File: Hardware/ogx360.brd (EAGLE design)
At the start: 97.1 x 36.5 mm, 29 parts, among them J1 USB_A_SMT_FEMALE_NS, SW1 TL3305AF160QG, U1 MAX3421ETQFP32-5MM, U2 74HC4050, U3 MIC5219-3.3YM5-TR, U4 ARDUINO_LEONARDO_MICRO, U5 ARDUINO_LEONARDO_MICRO, U6 ARDUINO_LEONARDO_MICRO, U7 ARDUINO_LEONARDO_MICRO, Y1 12MHz

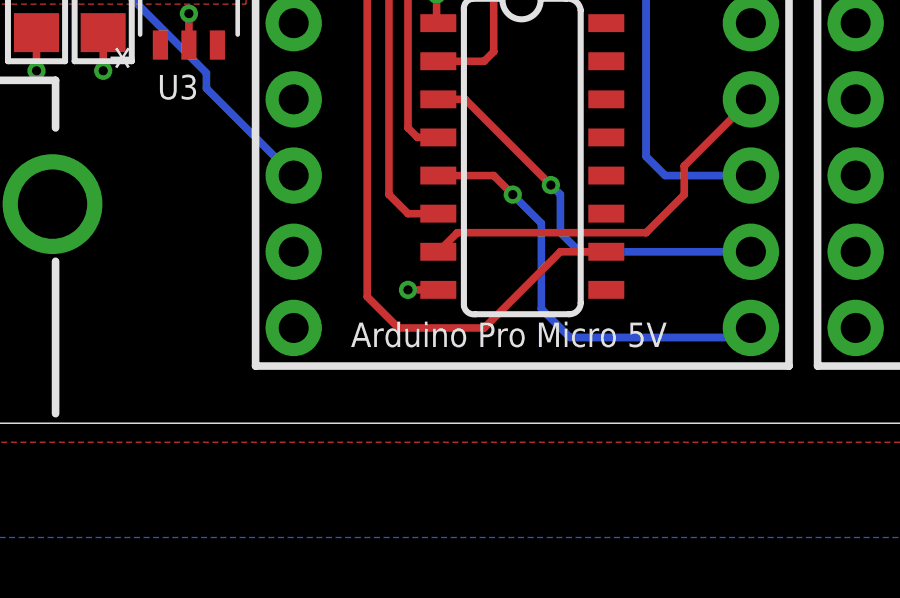
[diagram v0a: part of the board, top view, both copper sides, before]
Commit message: HW: Route reset trace
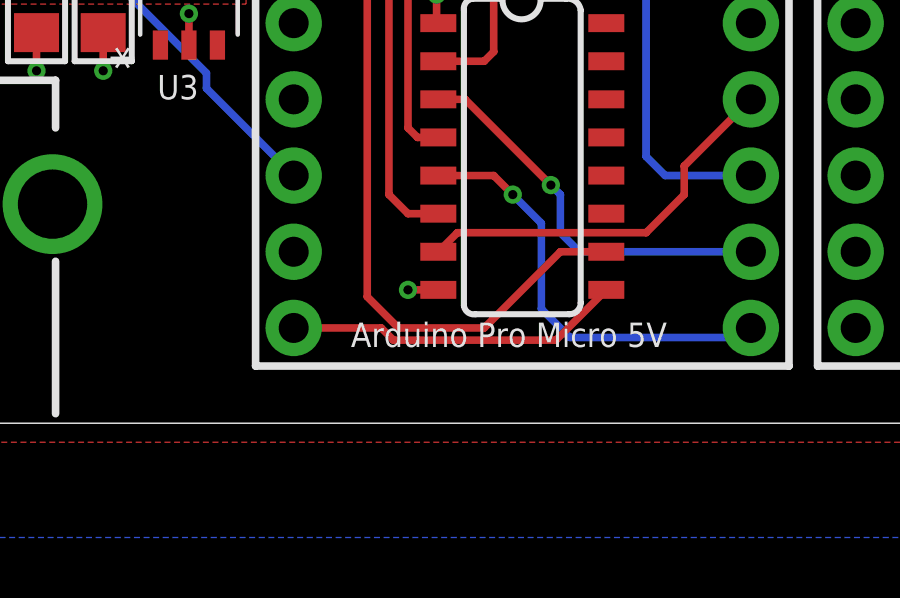
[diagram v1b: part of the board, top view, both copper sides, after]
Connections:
- removed net USB_RESET: U4.P$13
- net AT_RES: now also U4.P$13
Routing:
- net AT_RES: track 0.00 -> 11.3 mm
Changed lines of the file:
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@@
 <drawing>
 <settings>
-<setting alwaysvectorfont="yes"/>
+<setting alwaysvectorfont="no"/>
 <setting verticaltext="up"/>
 </settings>
@@
 </layers>
 <board>
-<fusionsync huburn="a.cGVyc29uYWw6dWUyZDg2Yzlk" projecturn="a.cGVyc29uYWw6dWUyZDg2YzlkIzIwMjAxMjEzMzYyMTgyMTMx" f3durn="urn:adsk.wipprod:dm.lineage:Cv0jk7A5QHWnhMoSxUJy-Q" pcbguid="" lastpulledtime="" lastsyncedchangeguid="1328549d-c9a3-a5b3-8ccd-199cf1c7b1e0" latestrevisionid="ccd092eb-6284-4767-97b7-4a64f160f77f" lastsyncedrevisionid="ccd092eb-6284-4767-97b7-4a64f160f77f" lastboardhashguid="f56ebee8-1ea0-2351-31bd-e778a8cae038" lastpushedtime="2020-12-14T08:00:36Z" linktopcb3d="true"/>
+<fusionsync huburn="a.cGVyc29uYWw6dWUyZDg2Yzlk" projecturn="a.cGVyc29uYWw6dWUyZDg2YzlkIzIwMjAxMjEzMzYyMTgyMTMx" f3durn="urn:adsk.wipprod:dm.lineage:Cv0jk7A5QHWnhMoSxUJy-Q" pcbguid="" lastpulledtime="" lastsyncedchangeguid="1328549d-c9a3-a5b3-8ccd-199cf1c7b1e0" latestrevisionid="ccd092eb-6284-4767-97b7-4a64f160f77f" lastsyncedrevisionid="ccd092eb-6284-4767-97b7-4a64f160f77f" lastboardhashguid="f56ebee8-1ea0-2351-31bd-e778a8cae038" lastpushedtime="2020-12-14T08:00:36Z" linktopcb3d="false"/>
 <plain>
 <wire x1="-0.3175" y1="0" x2="96.8175" y2="0" width="0" layer="20"/>
@@
 <wire x1="9.8425" y1="26.3525" x2="10.4808" y2="26.9908" width="0.254" layer="1"/>
 </signal>
-<signal name="USB_RESET">
-<contactref element="U4" pad="P$13"/>
-</signal>
 <signal name="VBCOMP">
 <contactref element="U1" pad="22"/>
@@
 <signal name="AT_RES">
 <contactref element="U2" pad="9"/>
+<contactref element="U4" pad="P$13"/>
+<wire x1="23.1775" y1="3.175" x2="26.0952625" y2="3.175" width="0.254" layer="1"/>
+<wire x1="26.0952625" y1="3.175" x2="26.5016625" y2="2.7686" width="0.254" layer="1"/>
+<wire x1="26.5016625" y1="2.7686" x2="31.9211" y2="2.7686" width="0.254" layer="1"/>
+<wire x1="31.9211" y1="2.7686" x2="33.5975" y2="4.445" width="0.254" layer="1"/>
 </signal>
 <signal name="MAX_MOSI">
